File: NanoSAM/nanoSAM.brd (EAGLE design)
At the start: 95.9 x 90.2 mm, 111 parts, among them J1 POWER_JACK, U1 LTC3260EMSEPBF, U2 LMV324

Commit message: changed a border for the A E S T H E T I C
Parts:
- R1: value 0 -> DNP
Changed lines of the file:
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@@
 <attribute name="VALUE" x="-20.27" y="-29.524" size="0.6096" layer="27" font="vector" ratio="20" align="top-left"/>
 </element>
-<element name="R1" library="SparkFun-Resistors" library_urn="urn:adsk.eagle:library:532" package="0805" package3d_urn="urn:adsk.eagle:package:39651/1" value="0" x="-19" y="-36" smashed="yes">
+<element name="R1" library="SparkFun-Resistors" library_urn="urn:adsk.eagle:library:532" package="0805" package3d_urn="urn:adsk.eagle:package:39651/1" value="DNP" x="-19" y="-36" smashed="yes">
 <attribute name="NAME" x="-19" y="-35.111" size="0.6096" layer="25" font="vector" ratio="20" align="bottom-center"/>
 <attribute name="PROD_ID" value=" " x="-19" y="-36" size="1.778" layer="27" display="off"/>

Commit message: Added HK Capacitors
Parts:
- added C34, C35, C36, C37, C38, C39, C40, C41: .1uF, SparkFun-Capacitors:0603
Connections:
- net DGND: now also C34.1, C35.1, C36.1, C37.1, C38.1, C39.1, C40.1, C41.1
- net HK_3V3_C: now also C40.2
- net HK_3V3_V: now also C41.2
- net HK_5V_C: now also C39.2
- net HK_BRD_THRM: now also C34.2
- net HK_INST_THRM0: now also C35.2
- net HK_INST_THRM1: now also C36.2
- net HK_INST_THRM2: now also C37.2
- net HK_INST_THRM3: now also C38.2
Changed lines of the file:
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@@
 <attribute name="VALUE" x="-19" y="-76.889" size="0.6096" layer="27" font="vector" ratio="20" align="top-center"/>
+</element>
+<element name="C34" library="SparkFun-Capacitors" library_urn="urn:adsk.eagle:library:510" package="0603" package3d_urn="urn:adsk.eagle:package:37414/1" value=".1uF" x="-19" y="-80" smashed="yes">
+<attribute name="NAME" x="-19" y="-79.238" size="0.6096" layer="25" font="vector" ratio="20" align="bottom-center"/>
+<attribute name="PROD_ID" value="CAP-08604" x="-19" y="-80" size="1.778" layer="27" display="off"/>
+<attribute name="VALUE" x="-19" y="-80.762" size="0.6096" layer="27" font="vector" ratio="20" align="top-center"/>
+</element>
+<element name="C35" library="SparkFun-Capacitors" library_urn="urn:adsk.eagle:library:510" package="0603" package3d_urn="urn:adsk.eagle:package:37414/1" value=".1uF" x="-19" y="-84" smashed="yes">
+<attribute name="NAME" x="-19" y="-83.238" size="0.6096" layer="25" font="vector" ratio="20" align="bottom-center"/>
+<attribute name="PROD_ID" value="CAP-08604" x="-19" y="-84" size="1.778" layer="27" display="off"/>
+<attribute name="VALUE" x="-19" y="-84.762" size="0.6096" layer="27" font="vector" ratio="20" align="top-center"/>
+</element>
+<element name="C36" library="SparkFun-Capacitors" library_urn="urn:adsk.eagle:library:510" package="0603" package3d_urn="urn:adsk.eagle:package:37414/1" value=".1uF" x="-19" y="-88" smashed="yes">
+<attribute name="NAME" x="-19" y="-87.238" size="0.6096" layer="25" font="vector" ratio="20" align="bottom-center"/>
+<attribute name="PROD_ID" value="CAP-08604" x="-19" y="-88" size="1.778" layer="27" display="off"/>
+<attribute name="VALUE" x="-19" y="-88.762" size="0.6096" layer="27" font="vector" ratio="20" align="top-center"/>
+</element>
+<element name="C37" library="SparkFun-Capacitors" library_urn="urn:adsk.eagle:library:510" package="0603" package3d_urn="urn:adsk.eagle:package:37414/1" value=".1uF" x="-19" y="-92" smashed="yes">
+<attribute name="NAME" x="-19" y="-91.238" size="0.6096" layer="25" font="vector" ratio="20" align="bottom-center"/>
+<attribute name="PROD_ID" value="CAP-08604" x="-19" y="-92" size="1.778" layer="27" display="off"/>
+<attribute name="VALUE" x="-19" y="-92.762" size="0.6096" layer="27" font="vector" ratio="20" align="top-center"/>
+</element>
+<element name="C38" library="SparkFun-Capacitors" library_urn="urn:adsk.eagle:library:510" package="0603" package3d_urn="urn:adsk.eagle:package:37414/1" value=".1uF" x="-19" y="-96" smashed="yes">
+<attribute name="NAME" x="-19" y="-95.238" size="0.6096" layer="25" font="vector" ratio="20" align="bottom-center"/>
+<attribute name="PROD_ID" value="CAP-08604" x="-19" y="-96" size="1.778" layer="27" display="off"/>
+<attribute name="VALUE" x="-19" y="-96.762" size="0.6096" layer="27" font="vector" ratio="20" align="top-center"/>
+</element>
+<element name="C39" library="SparkFun-Capacitors" library_urn="urn:adsk.eagle:library:510" package="0603" package3d_urn="urn:adsk.eagle:package:37414/1" value=".1uF" x="-19" y="-100" smashed="yes">
+<attribute name="NAME" x="-19" y="-99.238" size="0.6096" layer="25" font="vector" ratio="20" align="bottom-center"/>
+<attribute name="PROD_ID" value="CAP-08604" x="-19" y="-100" size="1.778" layer="27" display="off"/>
+<attribute name="VALUE" x="-19" y="-100.762" size="0.6096" layer="27" font="vector" ratio="20" align="top-center"/>
+</element>
+<element name="C40" library="SparkFun-Capacitors" library_urn="urn:adsk.eagle:library:510" package="0603" package3d_urn="urn:adsk.eagle:package:37414/1" value=".1uF" x="-19" y="-104" smashed="yes">
+<attribute name="NAME" x="-19" y="-103.238" size="0.6096" layer="25" font="vector" ratio="20" align="bottom-center"/>
+<attribute name="PROD_ID" value="CAP-08604" x="-19" y="-104" size="1.778" layer="27" display="off"/>
+<attribute name="VALUE" x="-19" y="-104.762" size="0.6096" layer="27" font="vector" ratio="20" align="top-center"/>
+</element>
+<element name="C41" library="SparkFun-Capacitors" library_urn="urn:adsk.eagle:library:510" package="0603" package3d_urn="urn:adsk.eagle:package:37414/1" value=".1uF" x="-19" y="-108" smashed="yes">
+<attribute name="NAME" x="-19" y="-107.238" size="0.6096" layer="25" font="vector" ratio="20" align="bottom-center"/>
+<attribute name="PROD_ID" value="CAP-08604" x="-19" y="-108" size="1.778" layer="27" display="off"/>
+<attribute name="VALUE" x="-19" y="-108.762" size="0.6096" layer="27" font="vector" ratio="20" align="top-center"/>
 </element>
 </elements>
@@
 <contactref element="U$12" pad="P7"/>
 <contactref element="U$2" pad="AGND"/>
+<contactref element="C34" pad="1"/>
+<contactref element="C40" pad="1"/>
+<contactref element="C39" pad="1"/>
+<contactref element="C38" pad="1"/>
+<contactref element="C37" pad="1"/>
+<contactref element="C36" pad="1"/>
+<contactref element="C35" pad="1"/>
+<contactref element="C41" pad="1"/>
 <wire x1="79" y1="86" x2="90.8" y2="85.1" width="0" layer="19" extent="1-1"/>
 <wire x1="71" y1="86" x2="79" y2="86" width="0" layer="19" extent="1-1"/>
@@
 <wire x1="-18.15" y1="-10" x2="32.845" y2="3.68" width="0" layer="19" extent="1-1"/>
 <wire x1="-19.85" y1="-14" x2="-18.15" y2="-10" width="0" layer="19" extent="1-1"/>
+<wire x1="-19.85" y1="-80" x2="-19.85" y2="-14" width="0" layer="19" extent="1-1"/>
+<wire x1="-19.85" y1="-84" x2="-19.85" y2="-80" width="0" layer="19" extent="1-1"/>
+<wire x1="-19.85" y1="-88" x2="-19.85" y2="-84" width="0" layer="19" extent="1-1"/>
+<wire x1="-19.85" y1="-92" x2="-19.85" y2="-88" width="0" layer="19" extent="1-1"/>
+<wire x1="-19.85" y1="-96" x2="-19.85" y2="-92" width="0" layer="19" extent="1-1"/>
+<wire x1="-19.85" y1="-100" x2="-19.85" y2="-96" width="0" layer="19" extent="1-1"/>
+<wire x1="-19.85" y1="-104" x2="-19.85" y2="-100" width="0" layer="19" extent="1-1"/>
+<wire x1="-19.85" y1="-108" x2="-19.85" y2="-104" width="0" layer="19" extent="1-1"/>
 </signal>
 <signal name="+3V3" class="2">
@@
 <wire x1="58.5" y1="27.25" x2="56.22" y2="29.53" width="0.254" layer="1"/>
 <wire x1="56.22" y1="29.53" x2="56.22" y2="37.19" width="0.254" layer="1"/>
+<contactref element="C40" pad="2"/>
+<wire x1="58.42" y1="25.845" x2="-18.15" y2="-104" width="0" layer="19" extent="1-1"/>
 </signal>
 <signal name="HK_3V3_V">
@@
 <wire x1="54.77" y1="34.5" x2="54.77" y2="32.91" width="0.254" layer="1"/>
 <wire x1="54.77" y1="32.91" x2="54.76" y2="32.9" width="0.254" layer="1"/>
+<contactref element="C41" pad="2"/>
+<wire x1="54.77" y1="32.91" x2="-18.15" y2="-108" width="0" layer="19" extent="1-1"/>
 </signal>
 <signal name="N$11">
@@
 <wire x1="57.16" y1="35.59" x2="48.59" y2="35.59" width="0.254" layer="16"/>
 <wire x1="37" y1="24" x2="48.59" y2="35.59" width="0.254" layer="16"/>
+<contactref element="C39" pad="2"/>
+<wire x1="35.1" y1="6.62" x2="-18.15" y2="-100" width="0" layer="19" extent="1-1"/>
 </signal>
 <signal name="N$23">
@@
 <wire x1="70.4" y1="34" x2="73.4" y2="31" width="0.254" layer="1"/>
 <wire x1="64.49" y1="34" x2="70.4" y2="34" width="0.254" layer="1"/>
+<contactref element="C34" pad="2"/>
+<wire x1="-18.15" y1="-80" x2="64.49" y2="34" width="0" layer="19" extent="1-1"/>
 </signal>
 <signal name="HK_INST_THRM1">
@@
 <wire x1="75" y1="57" x2="81.455" y2="63.455" width="0.254" layer="1"/>
 <wire x1="81.455" y1="63.455" x2="82.3" y2="63.455" width="0.254" layer="1"/>
+<contactref element="C36" pad="2"/>
 <wire x1="65.6" y1="83.4" x2="65.54" y2="86" width="0" layer="19" extent="1-1"/>
+<wire x1="-18.15" y1="-88" x2="71.46" y2="37.19" width="0" layer="19" extent="1-1"/>
 </signal>
 <signal name="HK_INST_THRM2">
@@
 <wire x1="78" y1="62" x2="78" y2="62.155" width="0.254" layer="1"/>
 <wire x1="78" y1="62.155" x2="76.7" y2="63.455" width="0.254" layer="1"/>
+<contactref element="C37" pad="2"/>
 <wire x1="73.6" y1="83.4" x2="73.54" y2="86" width="0" layer="19" extent="1-1"/>
+<wire x1="-18.15" y1="-92" x2="74" y2="37.19" width="0" layer="19" extent="1-1"/>
 </signal>
 <signal name="HK_INST_THRM3">
@@
 <wire x1="84" y1="63" x2="84" y2="67.5299875" width="0.254" layer="1"/>
 <wire x1="82.9949875" y1="68.535" x2="82.3" y2="68.535" width="0.254" layer="1"/>
+<contactref element="C38" pad="2"/>
 <wire x1="81.7" y1="83.4" x2="81.54" y2="86" width="0" layer="19" extent="1-1"/>
+<wire x1="-18.15" y1="-96" x2="76.54" y2="37.19" width="0" layer="19" extent="1-1"/>
 </signal>
 <signal name="HK_INST_THRM0">
@@
 <wire x1="74" y1="69" x2="76.075" y2="71.075" width="0.254" layer="1"/>
 <wire x1="76.075" y1="71.075" x2="76.7" y2="71.075" width="0.254" layer="1"/>
+<contactref element="C35" pad="2"/>
 <wire x1="59.6" y1="83.5" x2="59.54" y2="86" width="0" layer="19" extent="1-1"/>
+<wire x1="-18.15" y1="-84" x2="68.92" y2="37.19" width="0" layer="19" extent="1-1"/>
 </signal>
 <signal name="N$5">

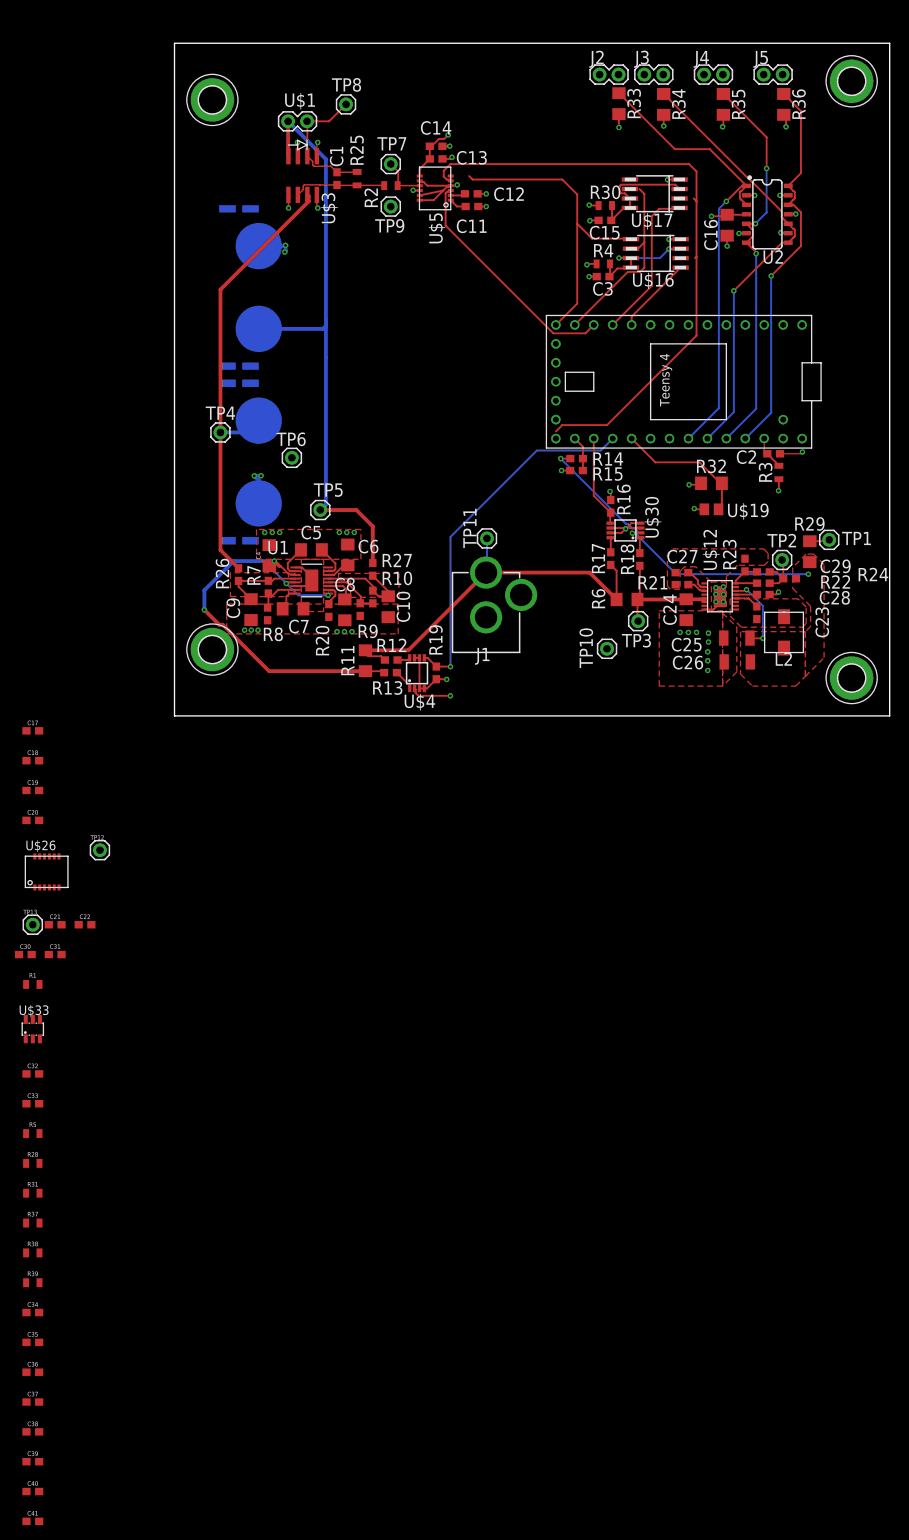
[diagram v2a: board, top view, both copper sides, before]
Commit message: added changes to PCB board layout including 3.3V linear regulator
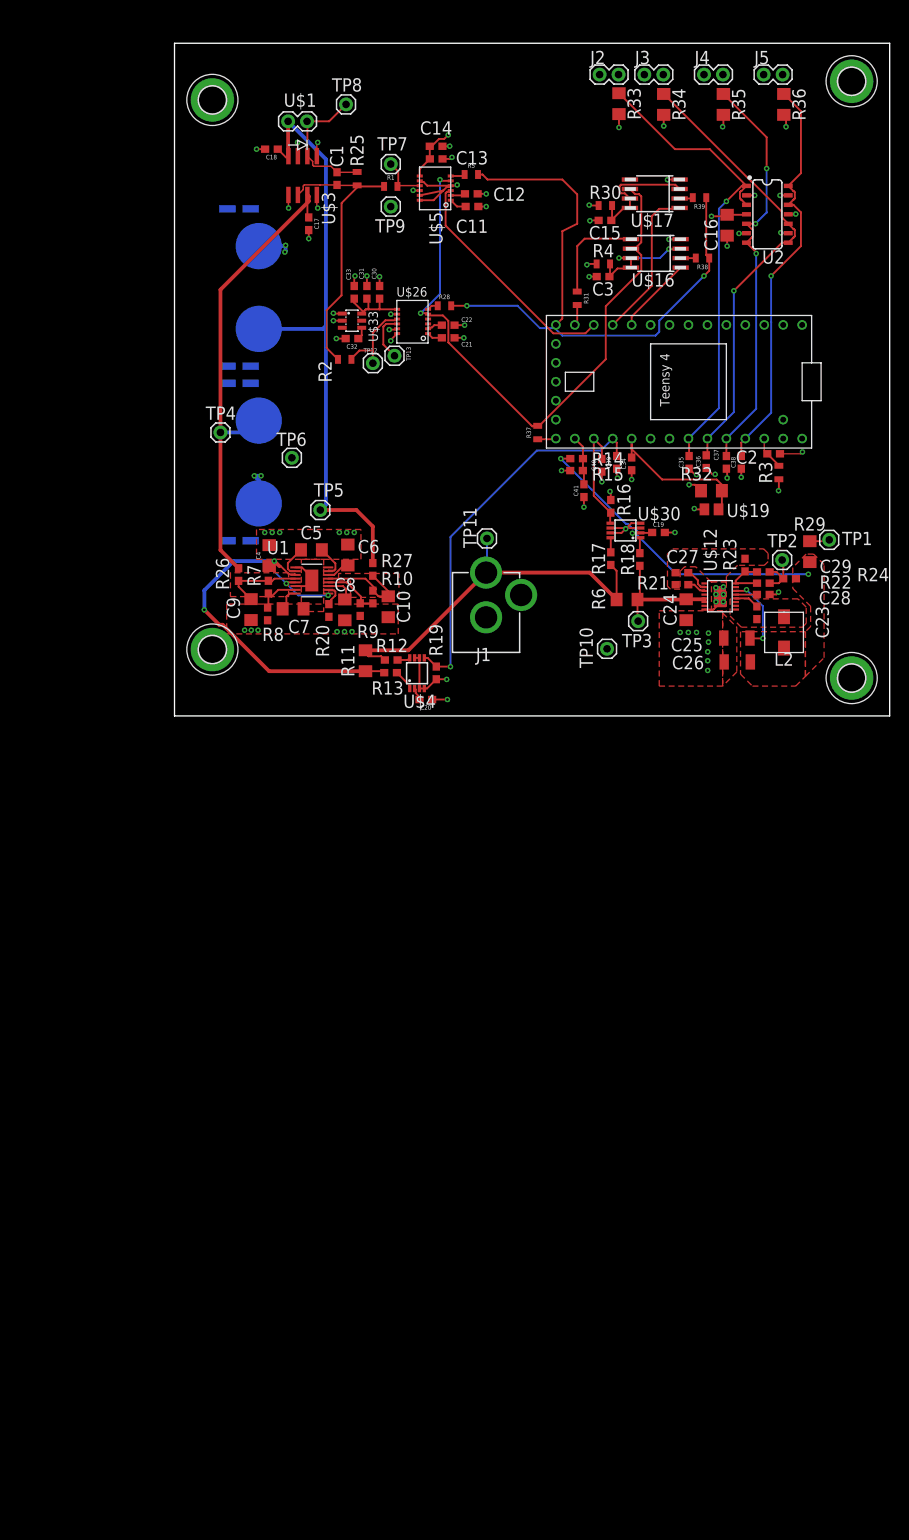
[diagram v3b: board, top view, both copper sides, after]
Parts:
- moved R39 170.8 mm to (70.4, 69.5), turned to 180 degrees
- moved C38 161.0 mm to (76.0, 34.0), turned to 90 degrees
- moved R38 160.8 mm to (70.8, 61.4), turned to 180 degrees
- moved C40 157.3 mm to (57.3, 33.6), turned to 90 degrees
- moved C41 156.7 mm to (54.9, 30.2), turned to 90 degrees
- moved C37 156.6 mm to (74.0, 34.0), turned to 90 degrees
- moved C39 155.2 mm to (59.3, 34.0), turned to 90 degrees
- moved C36 151.9 mm to (71.3, 34.1), turned to 90 degrees
- moved C35 147.2 mm to (69.0, 34.0), turned to 90 degrees
- moved R5 141.4 mm to (39.8, 72.6)
- moved R31 140.5 mm to (54.0, 56.0), turned to 270 degrees
- moved C34 139.3 mm to (61.3, 33.8), turned to 90 degrees
- moved R28 127.6 mm to (36.2, 55.0)
- moved R37 125.8 mm to (48.7, 38.0), turned to 90 degrees
- moved R1 117.3 mm to (29.0, 71.0)
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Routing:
- net SPI_MISO: track 42.2 -> 84.7 mm, vias 0 -> 2
- net N$2: track 12.5 -> 38.1 mm
- net N$38: track 25.4 -> 2.80 mm
- net AGND: track 23.3 -> 45.7 mm, vias 21 -> 34
- net DGND: track 59.5 -> 73.5 mm, vias 36 -> 46
- net SPI_MOSI: track 0.00 -> 13.8 mm
- net N$5: track 0.00 -> 11.5 mm
- net N$26: track 0.00 -> 10.3 mm
- net 5V: track 61.8 -> 66.6 mm
- net HK_3V3_C: track 12.3 -> 15.5 mm
- net HK_BRD_THRM: track 18.4 -> 21.5 mm
- net HK_INST_THRM3: track 52.8 -> 55.4 mm
- net HK_5V_C: track 48.6 -> 51.2 mm
- net N$39: track 0.00 -> 2.48 mm
- net HK_INST_THRM0: track 63.0 -> 65.4 mm
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
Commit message: fixed some PCB issues
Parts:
- C16: value .1uF -> 1uF; device SparkFun-Capacitors:1206 -> SparkFun-Capacitors:0603
- moved R2 20.9 mm to (24.5, 68.7), turned to 270 degrees
- moved TP12 15.0 mm to (24.5, 62.2)
- moved TP13 14.0 mm to (27.5, 62.2)
- moved C22 10.9 mm to (25.9, 51.1), turned to 90 degrees
- moved C21 8.91 mm to (27.8, 51.1), turned to 90 degrees
- moved C30 7.34 mm to (21.0, 60.2)
- moved C31 7.34 mm to (19.3, 60.2)
- moved C33 7.34 mm to (17.6, 60.2)
- moved R28 7.34 mm to (29.7, 58.4)
- moved C32 7.34 mm to (17.3, 54.0)
- moved U$26 7.34 mm to (27.5, 53.4)
- moved U$33 7.34 mm to (17.3, 56.4)
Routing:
- net HK_3V3_PG: track 0.00 -> 50.5 mm, vias 0 -> 1
- net N$2: track 38.1 -> 14.1 mm
- net ADC_CS: track 31.5 -> 54.9 mm
- net 5V: track 66.6 -> 81.4 mm
- net SPI_MOSI: track 13.8 -> 23.8 mm
- net SPI_SCK: track 83.4 -> 91.0 mm
- net N$35: track 0.00 -> 4.59 mm
- net +3V3: track 32.4 -> 36.6 mm, vias 11 -> 12
- net AGND: track 45.7 -> 48.9 mm, vias 34 -> 35
- net HK_INST_THRM3: track 55.4 -> 58.1 mm
- net HK_INST_THRM2: track 55.7 -> 58.3 mm
- net HK_INST_THRM1: track 61.2 -> 63.9 mm
- net HK_INST_THRM0: track 65.4 -> 67.9 mm
- net N$9: track 2.05 -> 4.24 mm
- net DGND: track 73.5 -> 75.7 mm
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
